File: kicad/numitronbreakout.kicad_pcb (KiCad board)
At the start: 4 copper layers, 60 x 100 mm, 12 parts, among them J1 Conn_01x06, U1 HV5812WG-G, U2 LM317_TO-220, U3 LM317_TO-220, U4 IV-12, U5 IV-12

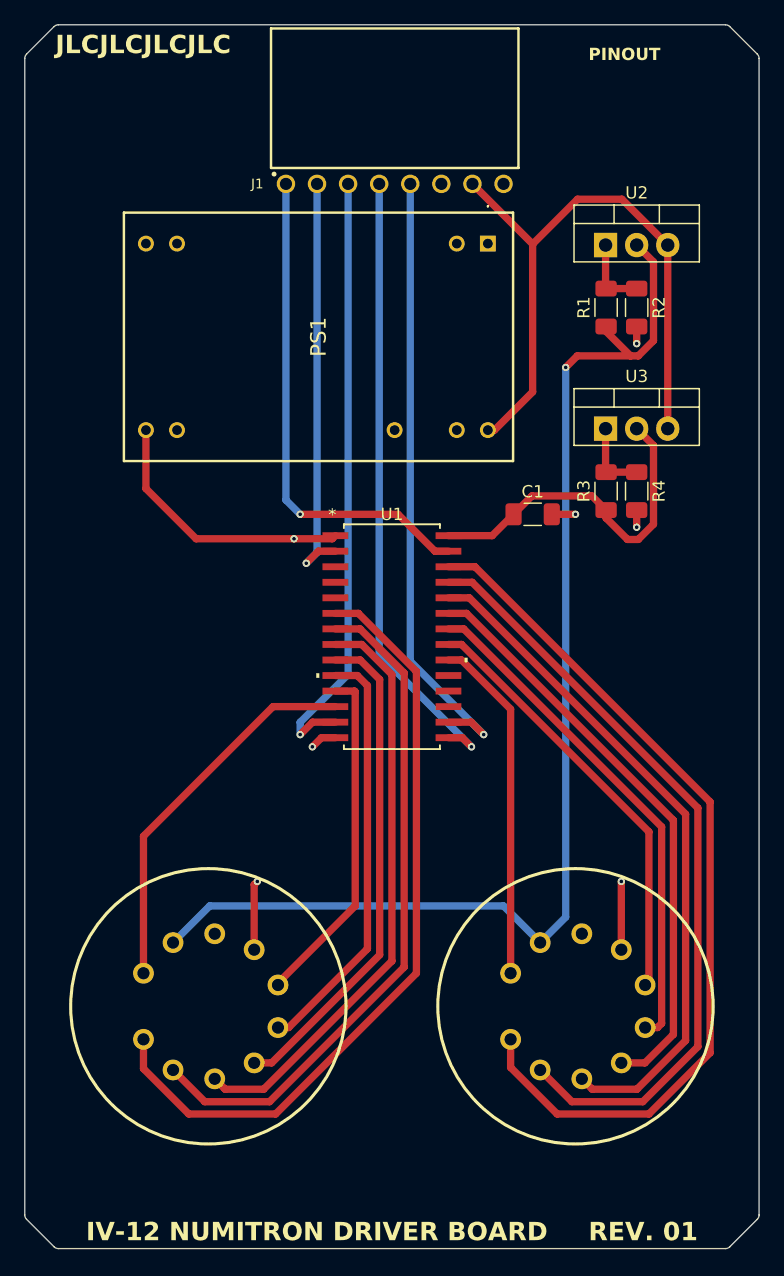
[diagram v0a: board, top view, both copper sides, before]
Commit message: updated boost converter and added dimming capability
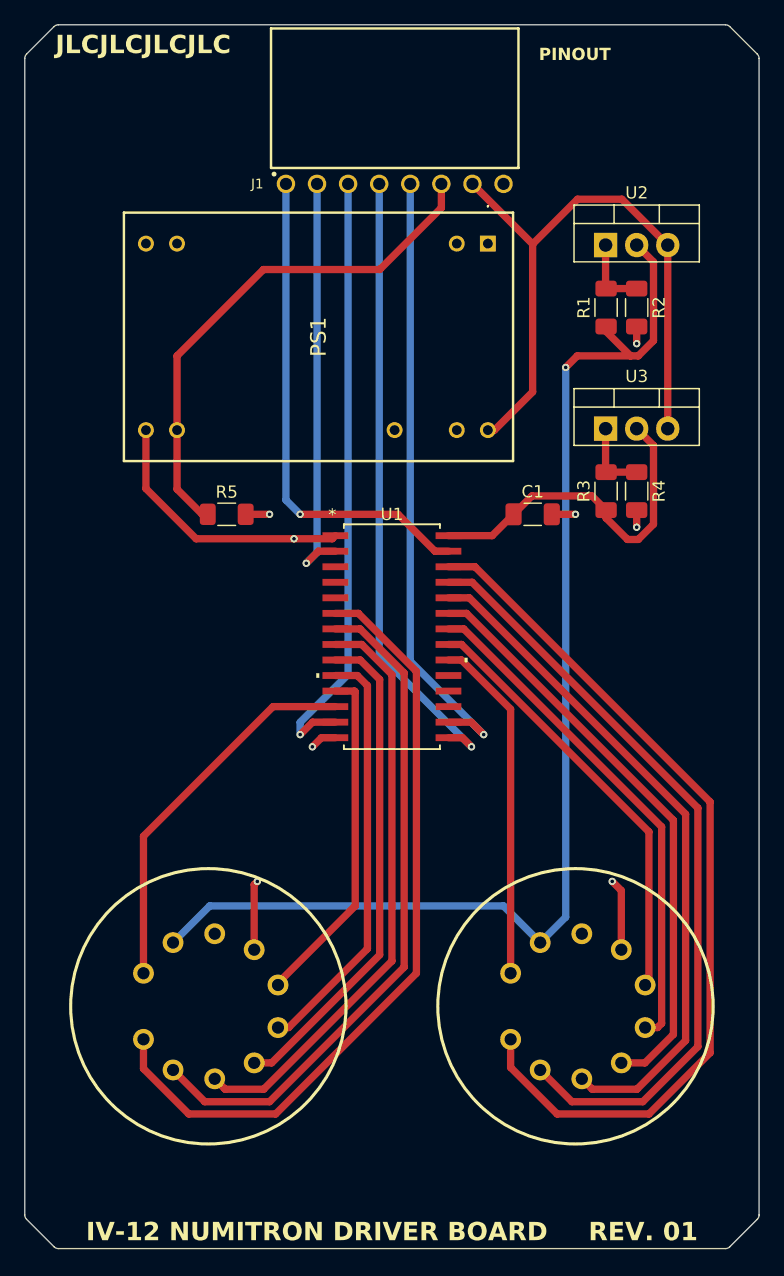
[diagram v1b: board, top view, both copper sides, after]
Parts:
- added R5: 1 kΩ, Resistor_SMD:R_1206_3216Metric_Pad1.30x1.75mm_HandSolder, F.Cu at (136.5, 90.0)
- PS1: value LDB-600L -> LDB-500L
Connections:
- J1 pad 6: unconnected-(J1-Pin_6-Pad6) -> DIMMING
- PS1 pad 14: unconnected-(PS1-+VOUT_2-Pad14) -> DIMMING
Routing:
- net DIMMING: track 0.00 -> 42.8 mm
- net GND: track 6.92 -> 8.37 mm, vias 4 -> 5

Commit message: added mounting holes
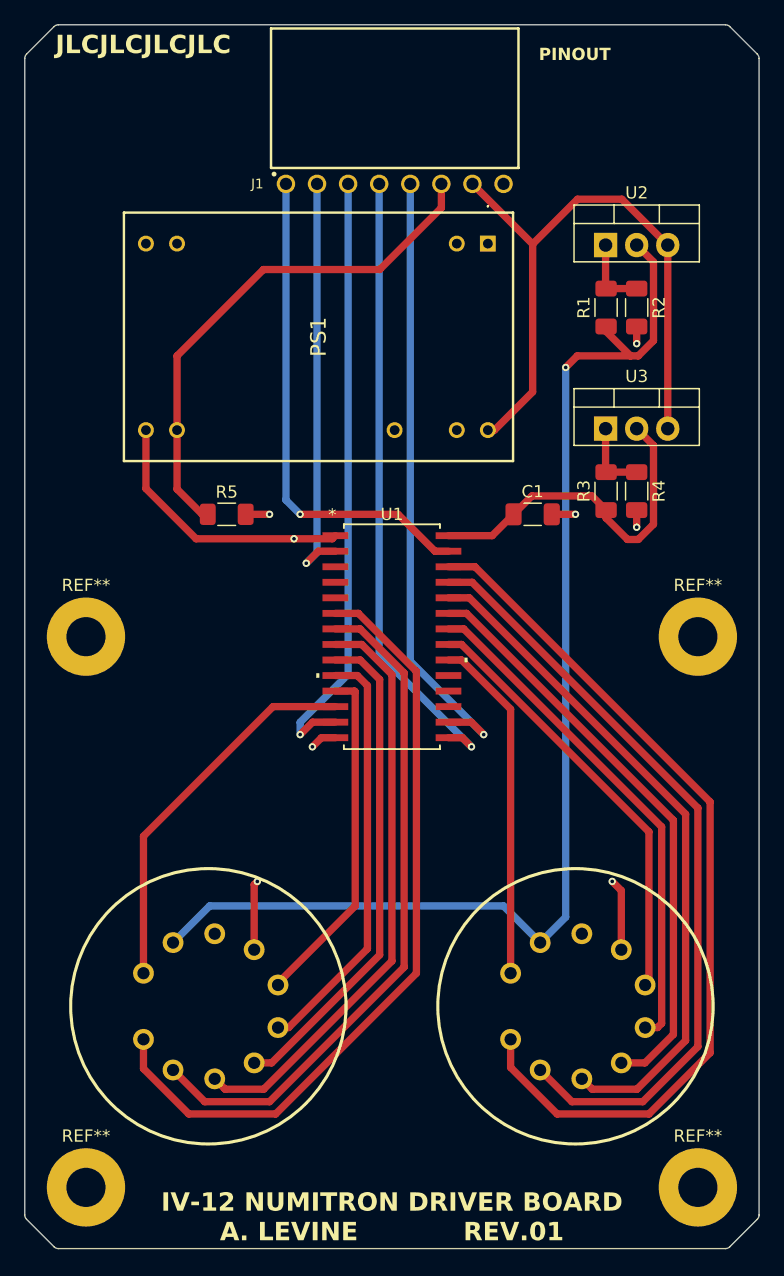
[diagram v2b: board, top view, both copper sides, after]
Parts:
- added REF**: MountingHole_3.2mm_M3_Pad, MountingHole:MountingHole_3.2mm_M3_Pad, F.Cu at (175.0, 100.0)
- added REF**: MountingHole_3.2mm_M3_Pad, MountingHole:MountingHole_3.2mm_M3_Pad, F.Cu at (125.0, 145.0)
- added REF**: MountingHole_3.2mm_M3_Pad, MountingHole:MountingHole_3.2mm_M3_Pad, F.Cu at (125.0, 100.0)
- added REF**: MountingHole_3.2mm_M3_Pad, MountingHole:MountingHole_3.2mm_M3_Pad, F.Cu at (175.0, 145.0)
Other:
- board text added: "IV-12 NUMITRON DRIVER BOARD A. LEVINE REV.01"
- board text removed: "IV-12 NUMITRON DRIVER BOARD"
- board text removed: "REV. 01"
